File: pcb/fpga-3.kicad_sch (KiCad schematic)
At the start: 5 parts, among them U5 XC7A35T-FGG484

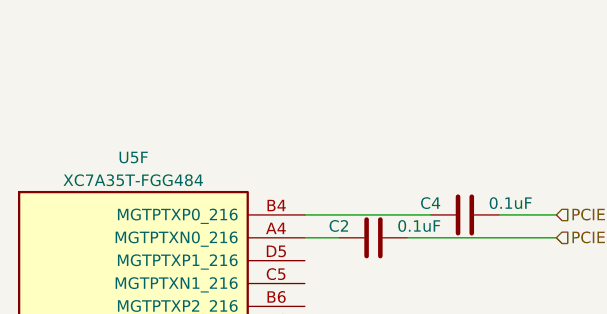
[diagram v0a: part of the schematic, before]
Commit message: current sense hierarchy definition
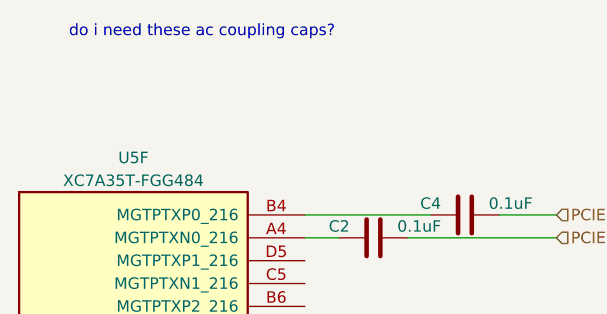
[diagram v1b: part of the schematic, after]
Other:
- note added: "do i need these ac coupling caps?"
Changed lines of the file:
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@@
 		(company "Andre S Winkel")
+	)
+	(text "do i need these ac coupling caps?"
+		(exclude_from_sim no)
+		(at 132.08 46.99 0)
+		(effects
+			(font
+				(size 1.27 1.27)
+			)
+		)
 	)
 	(wire
@@
 			)
 		)
-		(property "Datasheet" ""
+		(property "Datasheet" "https://docs.amd.com/v/u/en-US/ds181_Artix_7_Data_Sheet"
 			(at 124.46 93.98 0)
 			(effects
@@
 					(size 1.27 1.27)
 				)
-			)
-		)
-		(property "Description" "Artix 7 T 35 XC7A35T-FGG484"
+				(hide yes)
+			)
+		)
+		(property "Description" "XC7A35T-FGG484"
 			(at 97.79 77.47 0)
 			(effects
 				(font
+					(size 1.27 1.27)
+				)
+				(hide yes)
+			)
+		)
+		(property "Name" ""
+			(at 124.46 93.98 0)
+			(effects
+				(font

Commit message: pcie definitions
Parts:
- removed C3, C5: 0.1uF, Capacitor_SMD:C_0402_1005Metric, symbol Device:C
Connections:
- net F2P_N: now reaches C2.1, U5.A4 (MGTPTXN0_216)
- net PCIE.P2F_N: now reaches U5.A8 (MGTPRXN0_216)
- net F2P_P: now reaches C4.1, U5.B4 (MGTPTXP0_216)
- net PCIE.P2F_P: now reaches U5.B8 (MGTPRXP0_216)
- net PCIE.TX_N renamed PCIE.F2P_N
- net PCIE.TX_P renamed PCIE.F2P_P
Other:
- note added: "https://pcisig.com/pci-express-base-specification-revision-20 https://www.renesas.com/en/document/gde/gen2-pcie-hardware-design-guide https://datasheets.raspberrypi.com/pcie/pcie-connector-standard.pdf"
- moved on the sheet: C2, C4

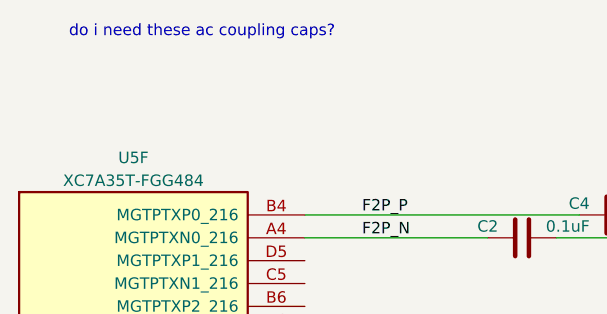
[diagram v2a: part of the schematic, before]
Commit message: added dram, defined pcie sideband sigs.
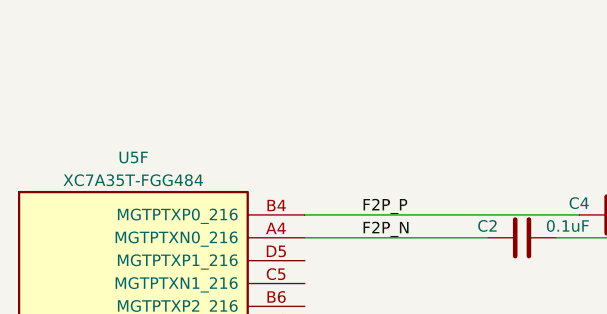
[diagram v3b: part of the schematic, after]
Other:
- note removed: "do i need these ac coupling caps?"
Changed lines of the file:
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@@
-		)
-	)
-	(text "do i need these ac coupling caps?"
-		(exclude_from_sim no)
-		(at 132.08 46.99 0)
-		(effects
-			(font
-				(size 1.27 1.27)
-			)
 		)
 	)

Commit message: saved libraries to project
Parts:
- C2, C4: symbol Device:C -> library:C
- U5: symbol FPGA_Xilinx_Artix7:XC7A35T-FGG484 -> library:XC7A35T-FGG484
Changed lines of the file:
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@@
 	)
 	(symbol
-		(lib_id "Device:C")
+		(lib_id "library:C")
 		(at 167.64 69.85 90)
 		(unit 1)
@@
 	)
 	(symbol
-		(lib_id "FPGA_Xilinx_Artix7:XC7A35T-FGG484")
+		(lib_id "library:XC7A35T-FGG484")
 		(at 124.46 93.98 0)
 		(unit 6)
@@
 	)
 	(symbol
-		(lib_id "Device:C")
+		(lib_id "library:C")
 		(at 177.8 67.31 90)
 		(unit 1)

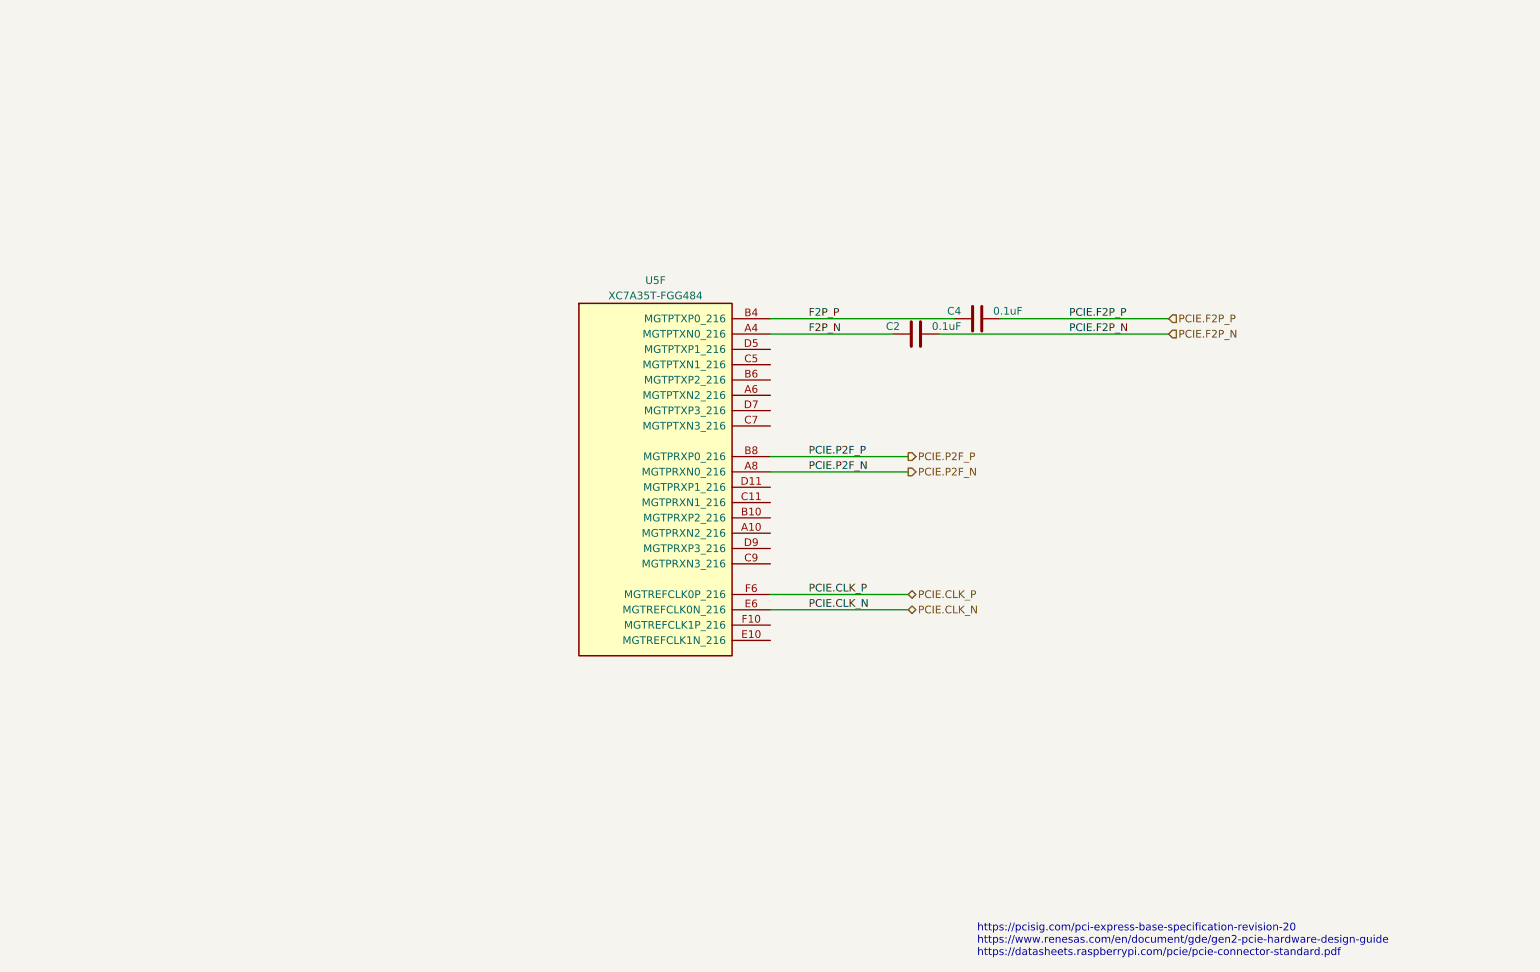
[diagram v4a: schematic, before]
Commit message: defined memory pinouts
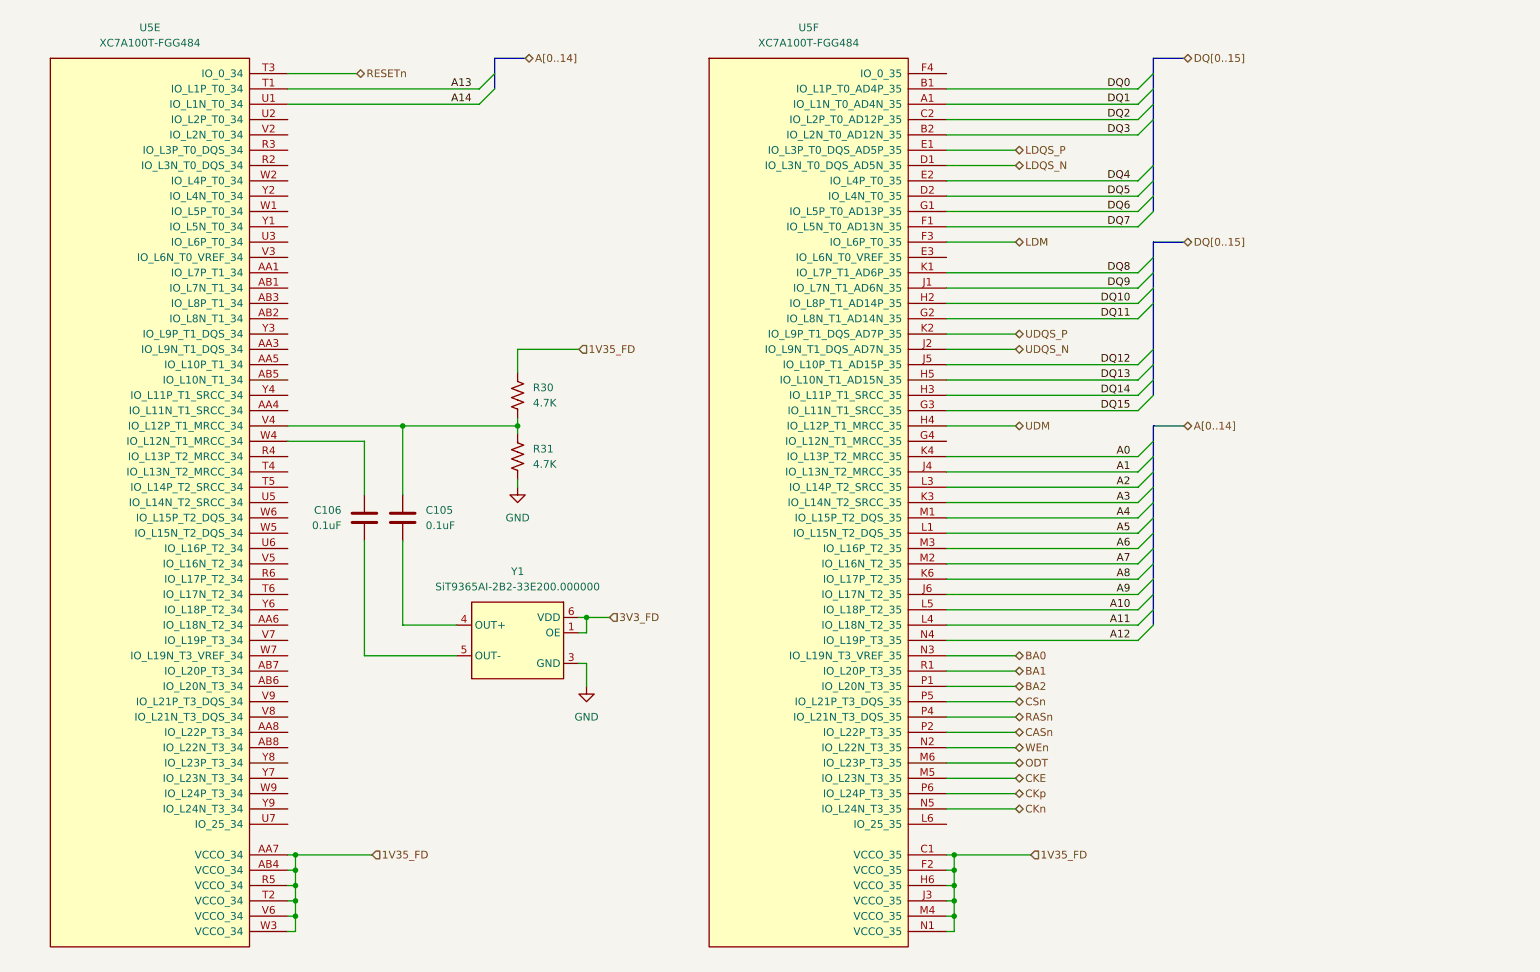
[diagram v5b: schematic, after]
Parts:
- removed C2, C4: 0.1uF, Capacitor_SMD:C_0402_1005Metric, symbol library:C
- removed U5: XC7A35T-FGG484, Package_BGA:Xilinx_FGG484, symbol library:XC7A35T-FGG484
- added C105, C106: 0.1uF, Capacitor_SMD:C_0201_0603Metric, symbol library:C
- added R30, R31: 4.7K, Resistor_SMD:R_0402_1005Metric, symbol library:R_US
- added U5: XC7A100T-FGG484, library:Xilinx_FGG484, symbol FPGA_Xilinx_Artix7:XC7A100T-FGG484
- added Y1: SiT9365AI-2B2-33E200.000000, Oscillator:Oscillator_SMD_SiTime_PQFD-6L_3.2x2.5mm, symbol Oscillator:SiT9365xx-xBx-xxE
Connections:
- new net: C105.2, R30.2, R31.1, U5.V4 (IO_L12P_T1_MRCC_34)
- new net: C106.2, U5.W4 (IO_L12N_T1_MRCC_34)
- new net: C105.1, Y1.4 (OUT+)
- new net: C106.1, Y1.5 (OUT-)
- new net 1V35_FD: R30.1, U5.AA7 (VCCO_34), U5.AB4 (VCCO_34), U5.C1 (VCCO_35), U5.F2 (VCCO_35), U5.H6 (VCCO_35), U5.J3 (VCCO_35), U5.M4 (VCCO_35), U5.N1 (VCCO_35), U5.R5 (VCCO_34), U5.T2 (VCCO_34), U5.V6 (VCCO_34), U5.W3 (VCCO_34)
- new net 3V3_FD: Y1.1 (OE), Y1.6 (VDD)
- new net A0: U5.K4 (IO_L13P_T2_MRCC_35)
- new net A1: U5.J4 (IO_L13N_T2_MRCC_35)
- new net A10: U5.L5 (IO_L18P_T2_35)
- new net A11: U5.L4 (IO_L18N_T2_35)
- new net A12: U5.N4 (IO_L19P_T3_35)
- new net A13: U5.T1 (IO_L1P_T0_34)
- new net A14: U5.U1 (IO_L1N_T0_34)
- new net A2: U5.L3 (IO_L14P_T2_SRCC_35)
- new net A3: U5.K3 (IO_L14N_T2_SRCC_35)
- new net A4: U5.M1 (IO_L15P_T2_DQS_35)
- new net A5: U5.L1 (IO_L15N_T2_DQS_35)
- new net A6: U5.M3 (IO_L16P_T2_35)
- new net A7: U5.M2 (IO_L16N_T2_35)
- new net A8: U5.K6 (IO_L17P_T2_35)
- new net A9: U5.J6 (IO_L17N_T2_35)
- new net BA0: U5.N3 (IO_L19N_T3_VREF_35)
- new net BA1: U5.R1 (IO_L20P_T3_35)
- new net BA2: U5.P1 (IO_L20N_T3_35)
- new net CASn: U5.P2 (IO_L22P_T3_35)
- new net CKE: U5.M5 (IO_L23N_T3_35)
- new net CKn: U5.N5 (IO_L24N_T3_35)
- new net CKp: U5.P6 (IO_L24P_T3_35)
- new net CSn: U5.P5 (IO_L21P_T3_DQS_35)
- new net DQ0: U5.B1 (IO_L1P_T0_AD4P_35)
- new net DQ1: U5.A1 (IO_L1N_T0_AD4N_35)
- new net DQ10: U5.H2 (IO_L8P_T1_AD14P_35)
- new net DQ11: U5.G2 (IO_L8N_T1_AD14N_35)
- new net DQ12: U5.J5 (IO_L10P_T1_AD15P_35)
- new net DQ13: U5.H5 (IO_L10N_T1_AD15N_35)
- new net DQ14: U5.H3 (IO_L11P_T1_SRCC_35)
- new net DQ15: U5.G3 (IO_L11N_T1_SRCC_35)
- new net DQ2: U5.C2 (IO_L2P_T0_AD12P_35)
- new net DQ3: U5.B2 (IO_L2N_T0_AD12N_35)
- new net DQ4: U5.E2 (IO_L4P_T0_35)
- new net DQ5: U5.D2 (IO_L4N_T0_35)
- new net DQ6: U5.G1 (IO_L5P_T0_AD13P_35)
- new net DQ7: U5.F1 (IO_L5N_T0_AD13N_35)
- new net DQ8: U5.K1 (IO_L7P_T1_AD6P_35)
- new net DQ9: U5.J1 (IO_L7N_T1_AD6N_35)
- new net GND: R31.2, Y1.3 (GND)
- new net LDM: U5.F3 (IO_L6P_T0_35)
- new net LDQS_N: U5.D1 (IO_L3N_T0_DQS_AD5N_35)
- new net LDQS_P: U5.E1 (IO_L3P_T0_DQS_AD5P_35)
- new net ODT: U5.M6 (IO_L23P_T3_35)
- new net RASn: U5.P4 (IO_L21N_T3_DQS_35)
- new net RESETn: U5.T3 (IO_0_34)
- new net UDM: U5.H4 (IO_L12P_T1_MRCC_35)
- new net UDQS_N: U5.J2 (IO_L9N_T1_DQS_AD7N_35)
- new net UDQS_P: U5.K2 (IO_L9P_T1_DQS_AD7P_35)
- new net WEn: U5.N2 (IO_L22N_T3_35)
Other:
- note removed: "https://pcisig.com/pci-express-base-specification-revision-20 https://www.renesas.com/en/document/gde/gen2-pcie-hardware-design-guide https://datasheets.raspberrypi.com/pcie/pcie-connector-standard.pdf"

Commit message: power restructuring
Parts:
- removed C105, C106: 0.1uF, Capacitor_SMD:C_0201_0603Metric, symbol library:C
- removed unit 6 of U5
- added C10, C?: 0.1uF, Capacitor_SMD:C_0402_1005Metric, symbol library:C
- added unit 6 of U5
- U5: symbol FPGA_Xilinx_Artix7:XC7A100T-FGG484 -> library:XC7A100T-FGG484
- Y1: symbol Oscillator:SiT9365xx-xBx-xxE -> library:SiT9365xx-xBx-xxE
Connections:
- net 1V35_FD: now also U5.C1 (VCCO_35), U5.F2 (VCCO_35), U5.H6 (VCCO_35), U5.J3 (VCCO_35), U5.M4 (VCCO_35), U5.N1 (VCCO_35)
- net A0: now also U5.K4 (IO_L13P_T2_MRCC_35)
- net A1: now also U5.J4 (IO_L13N_T2_MRCC_35)
- net A10: now also U5.L5 (IO_L18P_T2_35)
- net A11: now also U5.L4 (IO_L18N_T2_35)
- net A12: now also U5.N4 (IO_L19P_T3_35)
- net A2: now also U5.L3 (IO_L14P_T2_SRCC_35)
- net A3: now also U5.K3 (IO_L14N_T2_SRCC_35)
- net A4: now also U5.M1 (IO_L15P_T2_DQS_35)
- net A5: now also U5.L1 (IO_L15N_T2_DQS_35)
- net A6: now also U5.M3 (IO_L16P_T2_35)
- net A7: now also U5.M2 (IO_L16N_T2_35)
- net A8: now also U5.K6 (IO_L17P_T2_35)
- net A9: now also U5.J6 (IO_L17N_T2_35)
- net BA0: now also U5.N3 (IO_L19N_T3_VREF_35)
- net BA1: now also U5.R1 (IO_L20P_T3_35)
- net BA2: now also U5.P1 (IO_L20N_T3_35)
- net CASn: now also U5.P2 (IO_L22P_T3_35)
- net CKE: now also U5.M5 (IO_L23N_T3_35)
- net CKn: now also U5.N5 (IO_L24N_T3_35)
- net CKp: now also U5.P6 (IO_L24P_T3_35)
- net CSn: now also U5.P5 (IO_L21P_T3_DQS_35)
- net DQ0: now also U5.B1 (IO_L1P_T0_AD4P_35)
- net DQ1: now also U5.A1 (IO_L1N_T0_AD4N_35)
- net DQ10: now also U5.H2 (IO_L8P_T1_AD14P_35)
- net DQ11: now also U5.G2 (IO_L8N_T1_AD14N_35)
- net DQ12: now also U5.J5 (IO_L10P_T1_AD15P_35)
- net DQ13: now also U5.H5 (IO_L10N_T1_AD15N_35)
- net DQ14: now also U5.H3 (IO_L11P_T1_SRCC_35)
- net DQ15: now also U5.G3 (IO_L11N_T1_SRCC_35)
- net DQ2: now also U5.C2 (IO_L2P_T0_AD12P_35)
- net DQ3: now also U5.B2 (IO_L2N_T0_AD12N_35)
- net DQ4: now also U5.E2 (IO_L4P_T0_35)
- net DQ5: now also U5.D2 (IO_L4N_T0_35)
- net DQ6: now also U5.G1 (IO_L5P_T0_AD13P_35)
- net DQ7: now also U5.F1 (IO_L5N_T0_AD13N_35)
- net DQ8: now also U5.K1 (IO_L7P_T1_AD6P_35)
- net DQ9: now also U5.J1 (IO_L7N_T1_AD6N_35)
- net LDM: now also U5.F3 (IO_L6P_T0_35)
- net LDQS_N: now also U5.D1 (IO_L3N_T0_DQS_AD5N_35)
- net LDQS_P: now also U5.E1 (IO_L3P_T0_DQS_AD5P_35)
- net ODT: now also U5.M6 (IO_L23P_T3_35)
- net RASn: now also U5.P4 (IO_L21N_T3_DQS_35)
- net UDM: now also U5.H4 (IO_L12P_T1_MRCC_35)
- net UDQS_N: now also U5.J2 (IO_L9N_T1_DQS_AD7N_35)
- net UDQS_P: now also U5.K2 (IO_L9P_T1_DQS_AD7P_35)
- net WEn: now also U5.N2 (IO_L22N_T3_35)
- net at R30.2, R31.1, U5.V4 (IO_L12P_T1_MRCC_34): now also C?.1
- net at U5.W4 (IO_L12N_T1_MRCC_34): now also C10.1
- net at Y1.4 (OUT+): now also C?.2
- net at Y1.5 (OUT-): now also C10.2
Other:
- moved on the sheet: R30, R31, U5E, Y1

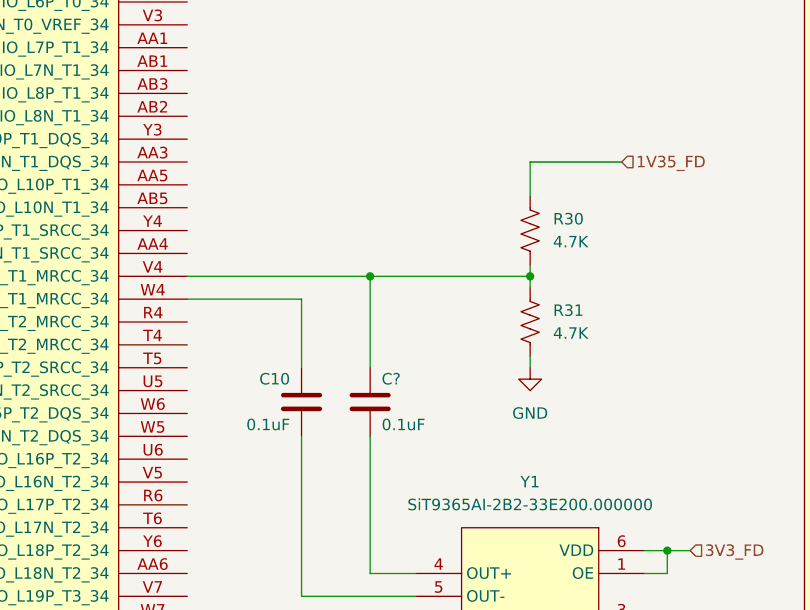
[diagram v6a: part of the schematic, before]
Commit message: changes to power tree
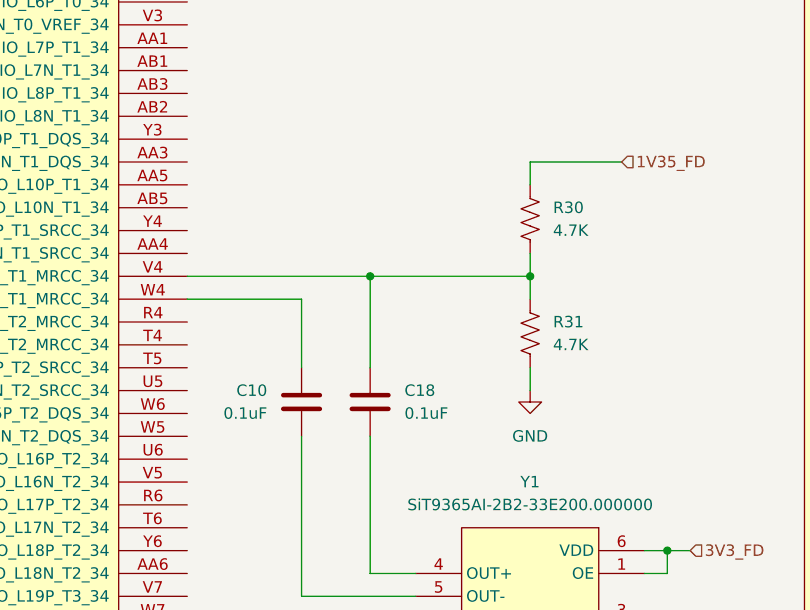
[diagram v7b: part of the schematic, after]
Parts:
- gave numbers to parts that had none: 1
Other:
- moved on the sheet: R30, R31
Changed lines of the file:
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@@
 	(wire
 		(pts
-			(xy 99.06 83.82) (xy 99.06 85.09)
+			(xy 99.06 83.82) (xy 99.06 86.36)
 		)
 		(stroke
@@
 	(wire
 		(pts
-			(xy 99.06 93.98) (xy 99.06 92.71)
+			(xy 99.06 96.52) (xy 99.06 93.98)
 		)
 		(stroke
@@
 	(wire
 		(pts
-			(xy 99.06 71.12) (xy 99.06 74.93)
+			(xy 99.06 71.12) (xy 99.06 73.66)
 		)
 		(stroke
@@
 		)
 	)
+	(wire
+		(pts
+			(xy 99.06 81.28) (xy 99.06 83.82)
+		)
+		(stroke
+			(width 0)
+			(type default)
+		)
+	)
 	(bus
 		(pts
@@
 	(wire
 		(pts
-			(xy 99.06 83.82) (xy 99.06 82.55)
-		)
-		(stroke
-			(width 0)
-			(type default)
-		)
-	)
-	(wire
-		(pts
 			(xy 172.72 96.52) (xy 205.74 96.52)
 		)
@@
 	(symbol
 		(lib_id "library:R_US")
-		(at 99.06 78.74 0)
+		(at 99.06 77.47 0)
 		(unit 1)
 		(exclude_from_sim no)
@@
 		(fields_autoplaced yes)
 		(property "Reference" "R30"
-			(at 101.6 77.4699 0)
+			(at 101.6 76.1999 0)
 			(effects
 				(font
@@
 		)
 		(property "Value" "4.7K"
-			(at 101.6 80.0099 0)
+			(at 101.6 78.7399 0)
 			(effects
 				(font
@@
 		)
 		(property "Footprint" "Resistor_SMD:R_0402_1005Metric"
-			(at 100.076 78.994 90)
+			(at 100.076 77.724 90)
 			(effects
 				(font
@@
 		)
 		(property "Datasheet" "~"
-			(at 99.06 78.74 0)
+			(at 99.06 77.47 0)
 			(effects
 				(font
@@
 		)
 		(property "Description" "Resistor, US symbol"
-			(at 99.06 78.74 0)
+			(at 99.06 77.47 0)
 			(effects
 				(font
@@
 	(symbol
 		(lib_id "library:R_US")
-		(at 99.06 88.9 0)
+		(at 99.06 90.17 0)
 		(unit 1)
 		(exclude_from_sim no)
@@
 		(fields_autoplaced yes)
 		(property "Reference" "R31"
-			(at 101.6 87.6299 0)
+			(at 101.6 88.8999 0)
 			(effects
 				(font
@@
 		)
 		(property "Value" "4.7K"
-			(at 101.6 90.1699 0)
+			(at 101.6 91.4399 0)
 			(effects
 				(font
@@
 		)
 		(property "Footprint" "Resistor_SMD:R_0402_1005Metric"
-			(at 100.076 89.154 90)
+			(at 100.076 90.424 90)
 			(effects
 				(font
@@
 		)
 		(property "Datasheet" "~"
-			(at 99.06 88.9 0)
+			(at 99.06 90.17 0)
 			(effects
 				(font
@@
 		)
 		(property "Description" "Resistor, US symbol"
-			(at 99.06 88.9 0)
+			(at 99.06 90.17 0)
 			(effects
 				(font
@@
 	(symbol
 		(lib_id "library:GND")
-		(at 99.06 93.98 0)
+		(at 99.06 96.52 0)
 		(unit 1)
 		(exclude_from_sim no)
@@
 		(fields_autoplaced yes)
 		(property "Reference" "#PWR038"
-			(at 99.06 100.33 0)
+			(at 99.06 102.87 0)
 			(effects
 				(font
@@
 		)
 		(property "Value" "GND"
-			(at 99.06 99.06 0)
+			(at 99.06 101.6 0)
 			(effects
 				(font
@@
 		)
 		(property "Footprint" ""
-			(at 99.06 93.98 0)
+			(at 99.06 96.52 0)
 			(effects
 				(font
@@
 		)
 		(property "Datasheet" ""
-			(at 99.06 93.98 0)
+			(at 99.06 96.52 0)
 			(effects
 				(font
@@
 		)
 		(property "Description" "Power symbol creates a global label with name \"GND\" , ground"
-			(at 99.06 93.98 0)
+			(at 99.06 96.52 0)
 			(effects
 				(font
@@
 		(on_board yes)
 		(dnp no)
-		(property "Reference" "C?"
-			(at 82.55 95.25 0)
+		(property "Reference" "C18"
+			(at 85.09 96.52 0)
 			(effects
 				(font
@@
 		)
 		(property "Value" "0.1uF"
-			(at 82.55 100.33 0)
+			(at 85.09 99.06 0)
 			(effects
 				(font
@@
 			(project "RPi-HwAB-1"
 				(path "/e63e39d7-6ac0-4ffd-8aa3-1841a4541b55/59d21473-a004-4514-8090-fd93db818925/143e814b-c088-43b0-8f2f-ada8c438e494"
-					(reference "C?")
+					(reference "C18")
 					(unit 1)
 				)
@@
 		(dnp no)
 		(property "Reference" "C10"
-			(at 72.39 95.25 0)
+			(at 69.85 96.52 0)
 			(effects
 				(font
@@
 		)
 		(property "Value" "0.1uF"
-			(at 72.39 100.33 0)
+			(at 69.85 99.06 0)
 			(effects
 				(font
